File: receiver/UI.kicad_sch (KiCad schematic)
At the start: 1 part

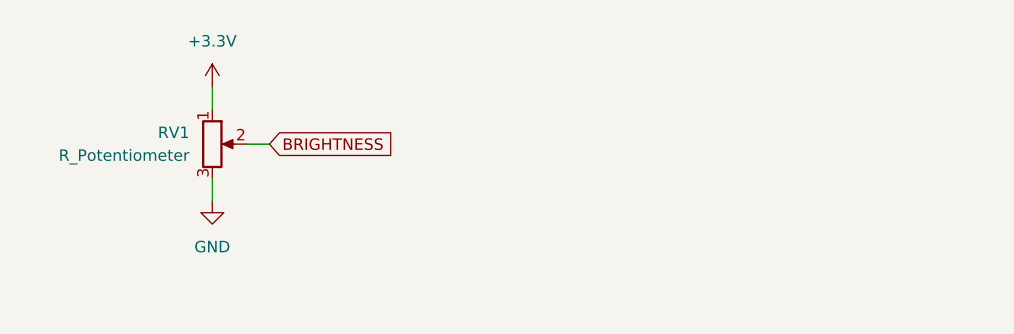
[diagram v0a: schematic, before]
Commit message: restored v1.7 of receiver, since 2.0 is abandoned
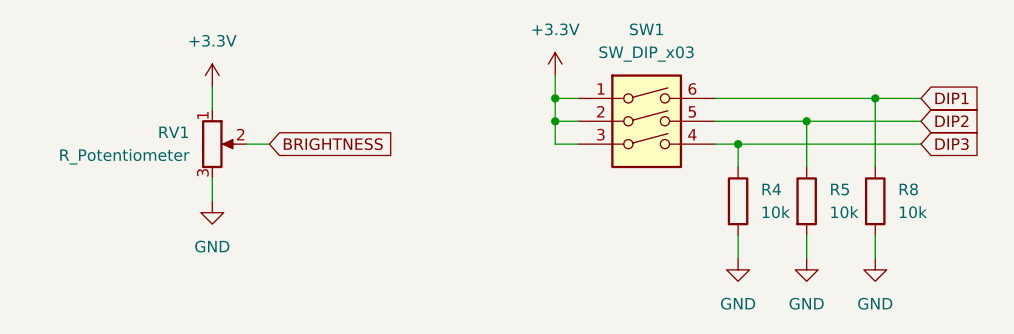
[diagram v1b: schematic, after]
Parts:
- added R4, R5, R8: 10k, Resistor_SMD:R_0805_2012Metric_Pad1.20x1.40mm_HandSolder, symbol Device:R
- added SW1: SW_DIP_x03, Button_Switch_SMD:SW_DIP_SPSTx03_Slide_6.7x9.18mm_W8.61mm_P2.54mm_LowProfile, symbol Switch:SW_DIP_x03
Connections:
- net +3.3V: now also SW1.1, SW1.2, SW1.3
- net GND: now also R4.2, R5.2, R8.2
- new net DIP1: R8.1, SW1.6
- new net DIP2: R5.1, SW1.5
- new net DIP3: R4.1, SW1.4

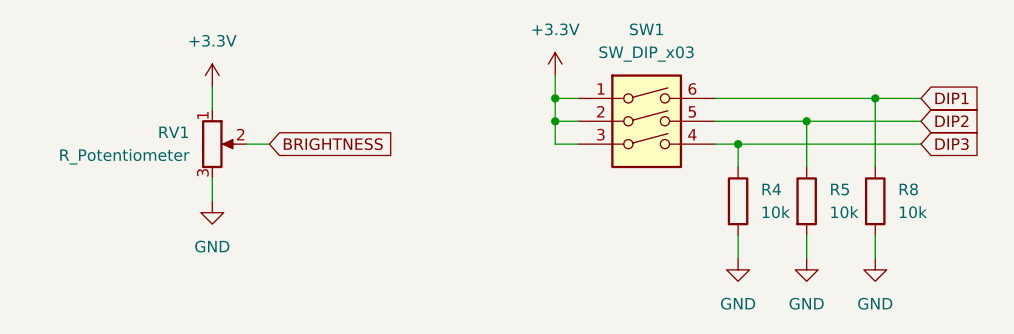
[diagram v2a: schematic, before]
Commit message: Finished first draft of new receiver
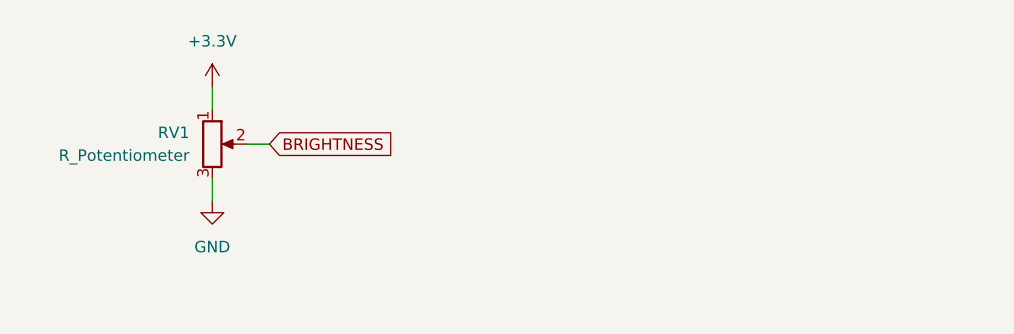
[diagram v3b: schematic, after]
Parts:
- removed R4, R5, R8: 10k, Resistor_SMD:R_0805_2012Metric_Pad1.20x1.40mm_HandSolder, symbol Device:R
- removed SW1: SW_DIP_x03, Button_Switch_SMD:SW_DIP_SPSTx03_Slide_6.7x9.18mm_W8.61mm_P2.54mm_LowProfile, symbol Switch:SW_DIP_x03
